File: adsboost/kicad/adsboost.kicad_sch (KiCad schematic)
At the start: 19 parts, among them J1 ANT_IN, J2 RF_OUT+BIAS, U1 TQP3M9036

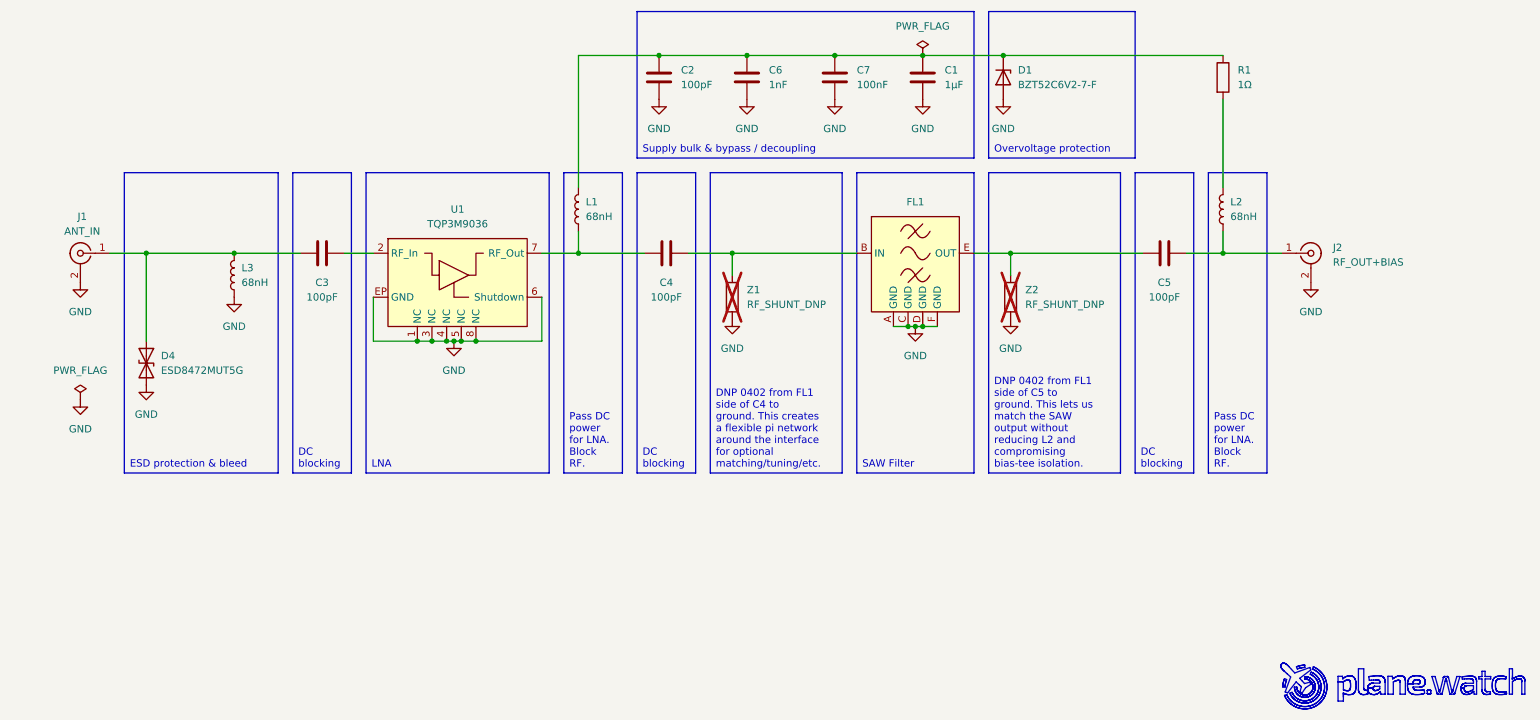
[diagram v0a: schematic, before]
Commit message: Add RF pi matching networks to ADSBoost
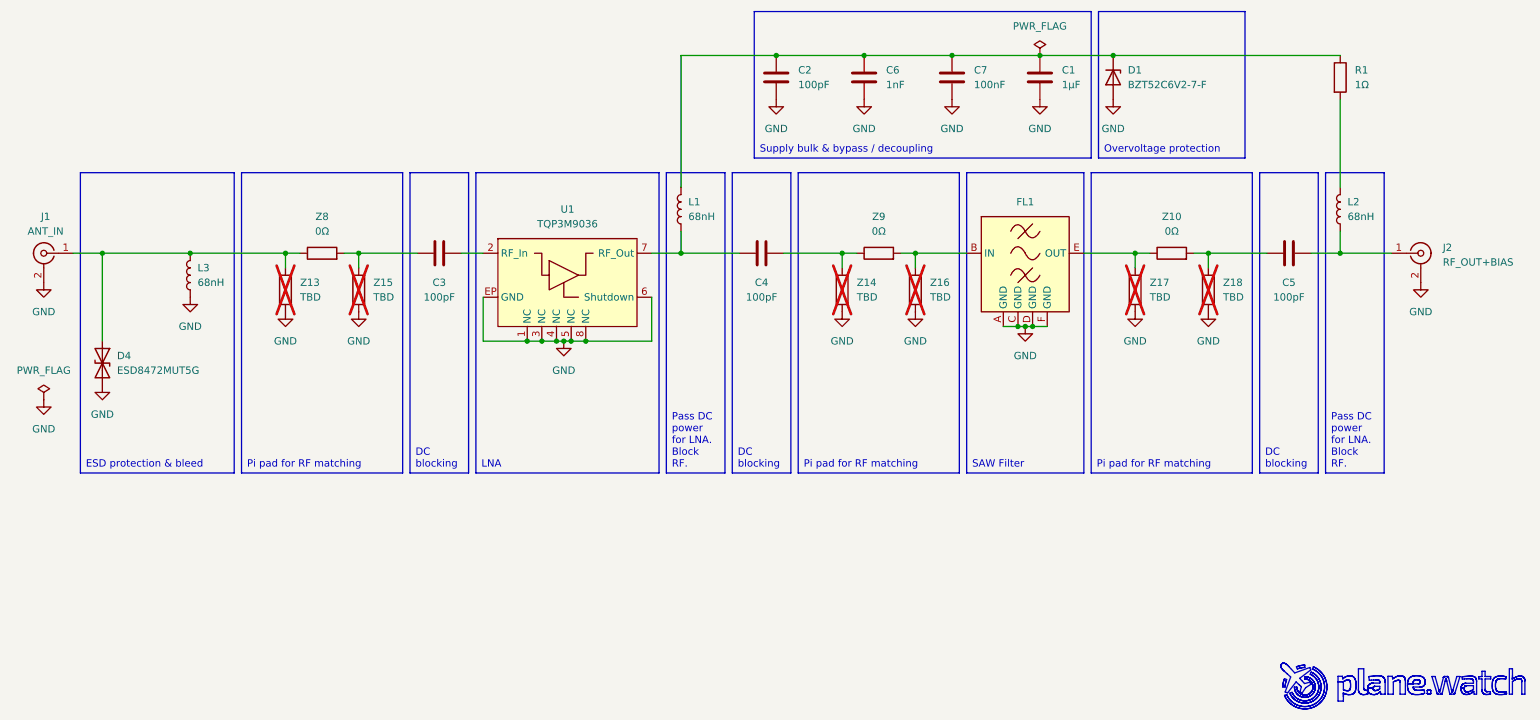
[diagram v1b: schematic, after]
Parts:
- removed Z1, Z2: RF_SHUNT_DNP, Resistor_SMD:R_0402_1005Metric, symbol Device:R
- added Z10, Z8, Z9: 0Ω, Resistor_SMD:R_0402_1005Metric, symbol Device:R
- added Z13, Z14, Z15, Z16, Z17, Z18: TBD, Resistor_SMD:R_0402_1005Metric, symbol Device:R
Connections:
- net GND: now also Z13.1, Z14.1, Z15.1, Z16.1, Z17.1, Z18.1
- net at D4.1 (A1), J1.1 (In), L3.2: now also Z13.2, Z8.1; no longer C3.2
- net at C4.1: now also Z14.2, Z9.1; no longer FL1.B (IN)
- net at C5.2: now also Z10.2, Z18.2; no longer FL1.E (OUT)
- new net: FL1.E (OUT), Z10.1, Z17.2
- new net: FL1.B (IN), Z16.2, Z9.2
- new net: C3.2, Z15.2, Z8.2
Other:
- moved on the sheet: C1, C2, C3, C4, C5, C6, C7, D1, D4, FL1, J1, J2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

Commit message: Add LCSC part numbers & descriptions
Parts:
- C1: lcsc_id (none) -> C528974
- C2, C3, C4, C5: lcsc_id (none) -> C2941926
- C6: lcsc_id (none) -> C126493
- C7: lcsc_id (none) -> C161163
- D1: lcsc_id (none) -> C397931
- J1, J2: lcsc_id (none) -> C3172723
- R1: lcsc_id (none) -> C313850
- U1: lcsc_id (none) -> C920261

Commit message: Fix C1 part number from 0402 to 0603 footprint
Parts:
- C1: lcsc_id C528974 -> C85862
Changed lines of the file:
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@@
 			)
 		)
-		(property "Description" "Murata Electronics, GRM155Z71A105KE01D"
+		(property "Description" "Murata Electronics, GCM188R71E105KA64D"
 			(at 200.66 64.77 0)
 			(hide yes)
@@
 			)
 		)
-		(property "lcsc_id" "C528974"
+		(property "lcsc_id" "C85862"
 			(at 200.66 64.77 0)
 			(hide yes)
